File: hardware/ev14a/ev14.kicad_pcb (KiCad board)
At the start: 4 copper layers, 94.4 x 80 mm, 165 parts, among them CN1 Conn_05x02_Female, CN2 PJ-242, J1 USB_C_Receptacle, J10 Conn_02x04_Odd_Even, J11 Conn_02x05_Counter_Clockwise, J2 Conn_01x02_Socket, J3 AudioJack4, J4 Conn_01x18, J5 Conn_02x03_Odd_Even, J7 Conn_02x05_Counter_Clockwise, J8 Conn_02x05_Counter_Clockwise, J9 Conn_02x05_Counter_Clockwise, Q1 2N7002, SW1 SW_SPDT, SW2 SW_Push, SW3 SW_Push, SW4 SW_Push, SW5 SW_Push, U1 BQ21040DBV, U10 STM32F405RGTx, U2 USBLC6-2P6, U3 STM32F072CBTx, U4 CH340C, U5 TPS63060, U6 WM8960CGEFL/RV, U7 ESP32-S3-WROOM-1, U8 M24C02-RMN6TP, U9 BM14B(0.8)-24DS-0.4V(53), Y1 Crystal_GND24

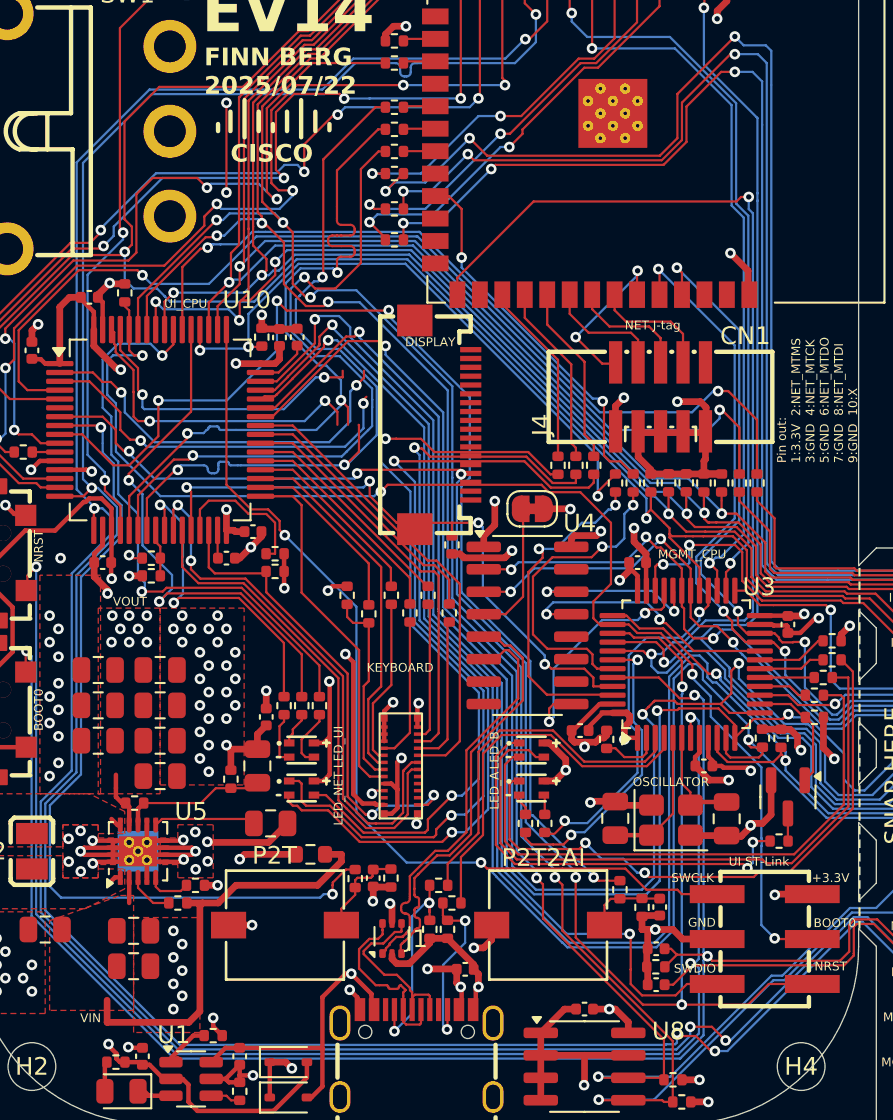
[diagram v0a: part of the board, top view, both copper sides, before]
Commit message: feat: move traces and add different fpc connector
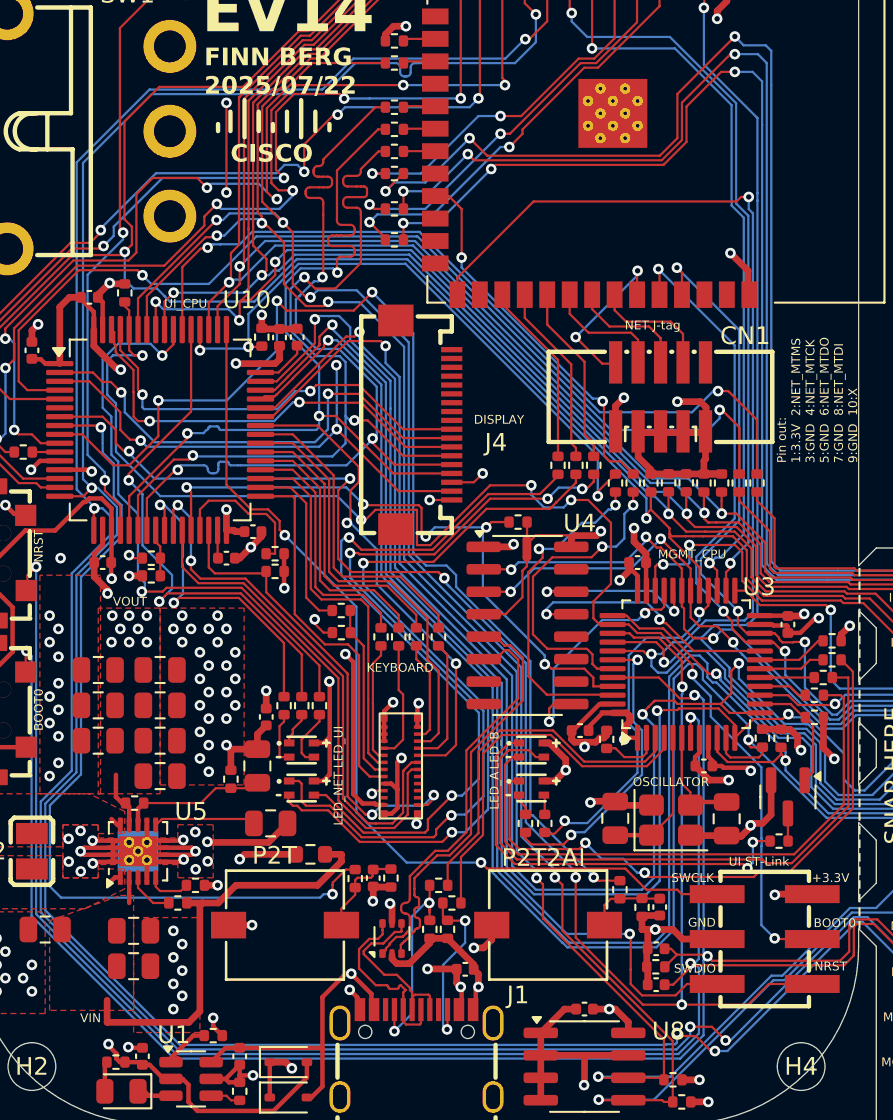
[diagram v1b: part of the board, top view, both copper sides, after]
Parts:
- removed JP1: SolderJumper_2_Bridged, Jumper:SolderJumper-2_P1.3mm_Bridged_RoundedPad1.0x1.5mm
- added NT2: NetTie_2, NetTie:NetTie-2_SMD_Pad0.5mm, F.Cu at (205.5, 100.5)
- J4: value Conn_01x18 -> Conn_01x18_MountingPin
- moved R41 3.96 mm to (205.0, 99.0), turned to 180 degrees
- moved R52 2.44 mm to (199.2, 105.5)
- moved R48 2.42 mm to (197.2, 105.5)
- moved R43 2.13 mm to (195.0, 105.2), turned to 0 degrees
- moved R47 1.57 mm to (195.0, 104.0), turned to 180 degrees
- moved R51 1.49 mm to (198.2, 105.5)
- moved R53 1.48 mm to (200.5, 105.5)
- moved J4 1.07 mm to (199.7, 93.5)
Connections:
- J4 pad 1: +3.3V -> (no net)
- J4 pad 10: unconnected-(J4-Pin_10-Pad10) -> /DISP_CS
- J4 pad 11: unconnected-(J4-Pin_11-Pad11) -> /DISP_RST
- J4 pad 12: unconnected-(J4-Pin_12-Pad12) -> /DISP_DC
- J4 pad 13: unconnected-(J4-Pin_13-Pad13) -> /SPI1_MISO
- J4 pad 14: unconnected-(J4-Pin_14-Pad14) -> /SPI1_MOSI
- J4 pad 15: unconnected-(J4-Pin_15-Pad15) -> /SPI1_CLK
- J4 pad 16: unconnected-(J4-Pin_16-Pad16) -> GND
- J4 pad 17: unconnected-(J4-Pin_17-Pad17) -> /DISP_BL
- J4 pad 18: unconnected-(J4-Pin_18-Pad18) -> +3.3V
- J4 pad 2: /DISP_BL -> (no net)
- J4 pad 3: GND -> (no net)
- J4 pad 4: /SPI1_CLK -> (no net)
- J4 pad 5: /SPI1_MOSI -> (no net)
- J4 pad 6: /SPI1_MISO -> (no net)
- J4 pad 7: /DISP_DC -> (no net)
- J4 pad 8: /DISP_RST -> (no net)
- J4 pad 9: /DISP_CS -> (no net)
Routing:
- net /SPI1_MISO: track 39.6 -> 48.8 mm, vias 2 -> 3
- net /DISP_BL: track 21.9 -> 29.8 mm, vias 2 -> 3
- net /DISP_CS: track 17.4 -> 24.1 mm
- net /DISP_DC: track 18.5 -> 25.0 mm
- net /SPI1_CLK: track 43.4 -> 49.4 mm
- net /SPI1_MOSI: track 43.6 -> 49.4 mm
- net /DISP_RST: track 22.3 -> 27.7 mm
- net /UI_BOOT0: track 73.4 -> 78.0 mm, vias 4 -> 6
- net Net-(U10-PC7): track 12.6 -> 16.4 mm
- net Net-(U10-PB15): track 10.7 -> 14.1 mm
- net Net-(U4-V3): track 7.84 -> 4.94 mm
- net Net-(U10-PC9): track 15.4 -> 18.1 mm
- net /KB_COL2: track 9.43 -> 6.84 mm
- net Net-(U10-PC6): track 12.7 -> 15.2 mm
- net /KB_COL4: track 7.93 -> 5.86 mm
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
